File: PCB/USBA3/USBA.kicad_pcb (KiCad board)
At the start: 2 copper layers, 70 x 70 mm, 20 parts, among them J1 USB_A, U1 ESP32-PICO-MINI-02, U2 Barcode, U3 CH340X, U4 QR, U5 MD8942, U6 SHT40

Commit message: Order
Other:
- board text removed: "JLCJLCJLC"

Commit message: Tweak
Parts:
- R10: value 40k2 -> 39k2
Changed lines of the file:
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@@
         (effects (font (size 1 1) (thickness 0.15)))
     )
-    (fp_text value "40k2" (at 0 1.1 90 unlocked) (layer "F.Fab") hide
+    (fp_text value "39k2" (at 0 1.1 90 unlocked) (layer "F.Fab") hide
         (effects (font (size 1 1) (thickness 0.15)))
     )

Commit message: Library update
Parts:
- moved U6 0.36 mm to (94.7, 85.5)
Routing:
- net +3.3V: track 27.5 -> 28.0 mm
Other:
- board text added: "Made in China by JLCPCB"
- board text added: "SDA:20 SCL:7 RGB:22/21/19"
- board text removed: "${TITLE}"
- board text removed: "SDA: 20 SCL: 7 RGB: 22/21/19"
- board text removed: "This is an assembled printed circuit board. This is a component, with no case or leads. Snap off any extra blank panels. Use this part for your own projects as you wish. Made in China for Andrews & Arnold Ltd."
- board text removed: "usba.revk.uk"
- board text removed: "®"

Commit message: Swapped around a bit
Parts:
- moved R11 6.59 mm to (100.3, 82.8), turned to 90 degrees
- moved R9 6.55 mm to (102.8, 81.7), turned to 0 degrees
- moved L2 6.45 mm to (102.8, 88.2), turned to 0 degrees
- moved R10 6.37 mm to (105.3, 82.8), turned to -90 degrees
- moved C6 5.15 mm to (100.3, 84.8), turned to 90 degrees
- moved C7 4.85 mm to (105.3, 84.8)
- moved C4 3.27 mm to (98.2, 83.4), turned to 180 degrees
- moved U5 2.75 mm to (102.8, 83.5), turned to 0 degrees
- moved C8 1.26 mm to (102.8, 85.5), turned to 0 degrees
- moved U3 0.45 mm to (97.8, 87.2)
- moved U6 0.43 mm to (94.8, 85.9)
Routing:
- net DC: track 13.1 -> 16.5 mm
- net GND: track 8.17 -> 5.95 mm, vias 4 -> 6
- net +3.3V: track 28.0 -> 28.8 mm
- net Net-(J1-D-): track 10.7 -> 9.93 mm
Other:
- board text added: "RGB: 22/21/19"
- board text added: "SDA:20 SCL:7"
- board text removed: "SDA:20 SCL:7 RGB:22/21/19"

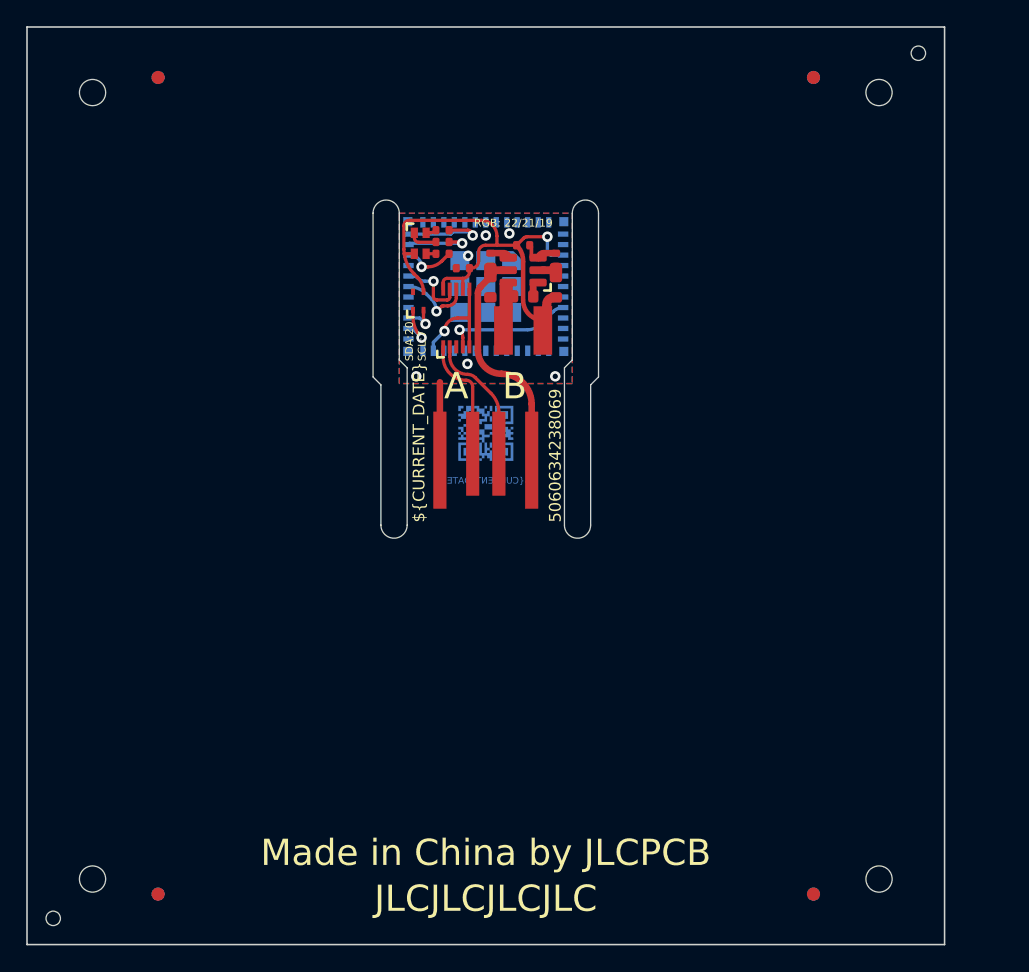
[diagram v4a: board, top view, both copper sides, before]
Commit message: Started rework for single sided
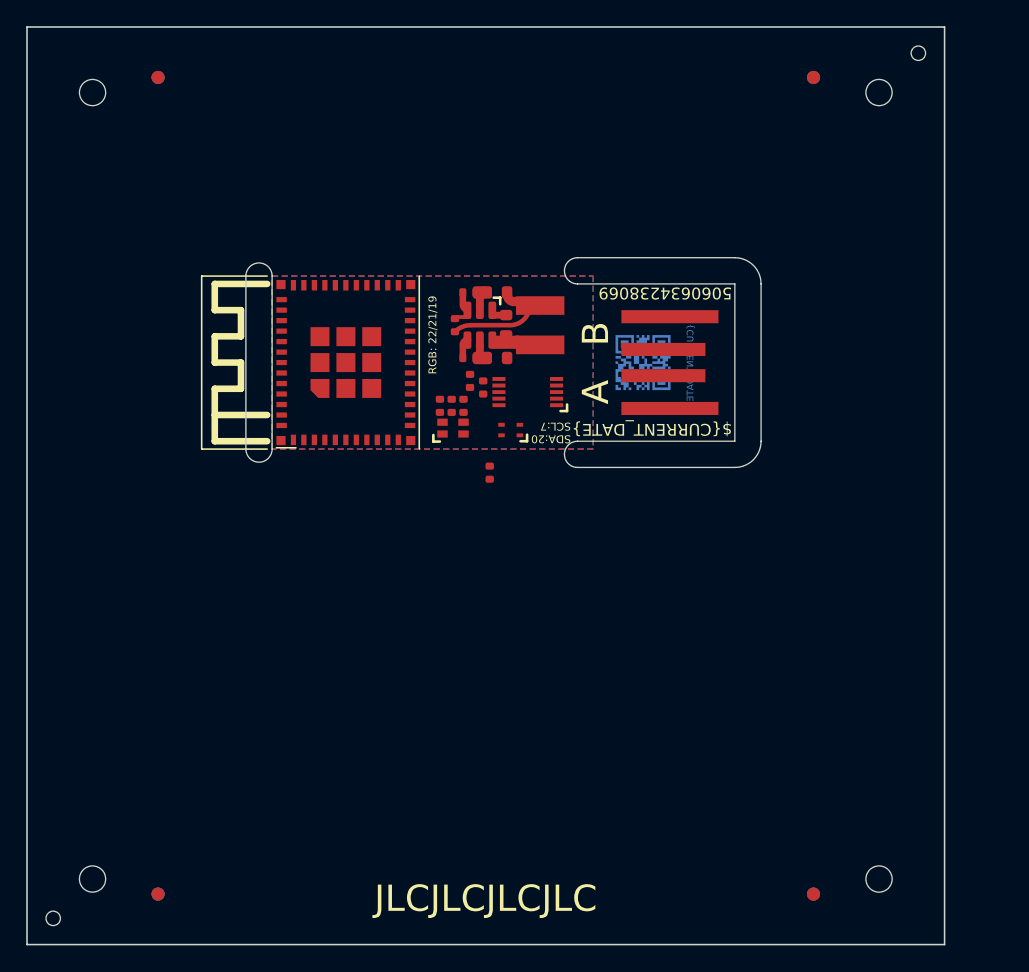
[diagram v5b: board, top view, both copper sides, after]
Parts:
- added C2: 10nF, RevK:C_0402, F.Cu at (100.3, 99.0)
- added C3: 100nF, RevK:C_0402, F.Cu at (99.8, 92.5)
- added V1: 70, RevK:VCUT70, F.Cu at (100.0, 84.0)
- added V2: 70, RevK:VCUT70, F.Cu at (100.0, 97.2)
- U1: moved to F.Cu
- moved J1 22.7 mm to (119.0, 90.6), turned to 90 degrees
- moved D2 14.3 mm to (97.5, 95.6), turned to 0 degrees
- moved R5 13.4 mm to (96.5, 93.9), turned to 90 degrees
- moved U4 13.2 mm to (112.0, 90.6), turned to -90 degrees
- moved R4 12.5 mm to (97.4, 93.9), turned to 90 degrees
- moved U1 12.1 mm to (89.3, 90.6), turned to 90 degrees
- moved U6 12.1 mm to (101.9, 95.8), turned to 180 degrees
- moved R7 11.7 mm to (98.3, 93.9), turned to 90 degrees
- moved C4 8.62 mm to (98.8, 92.0), turned to -90 degrees
- moved R9 8.02 mm to (97.7, 87.8), turned to 90 degrees
- moved U3 7.85 mm to (103.2, 92.8), turned to 180 degrees
- moved R11 7.67 mm to (98.8, 90.2), turned to 180 degrees
- moved R10 7.06 mm to (98.8, 85.2), turned to 0 degrees
- moved C6 5.42 mm to (100.8, 90.2), turned to 180 degrees
- moved U5 5.34 mm to (99.5, 87.8), turned to 90 degrees
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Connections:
- J1 pad 1: DC -> VBUS
- U3 pad 10: +3.3V -> Net-(U3-V3)
- U3 pad 7: +3.3V -> VBUS
- U5 pad 5: DC -> VBUS
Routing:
- net +3.3V: track 28.8 -> 0.00 mm, vias 1 -> 0
- net DC: track 16.5 -> 0.00 mm
- net Net-(J1-D-): track 9.93 -> 0.00 mm
- net EN: track 9.40 -> 0.00 mm, vias 1 -> 0
- net Net-(J1-D+): track 9.34 -> 0.00 mm
- net GPIO0: track 8.68 -> 0.00 mm, vias 1 -> 0
- net G: track 7.16 -> 0.00 mm, vias 1 -> 0
- net GND: track 5.95 -> 0.00 mm, vias 6 -> 0
- net I: track 5.73 -> 0.00 mm, vias 1 -> 0
- net O: track 5.30 -> 0.00 mm, vias 1 -> 0
- net R: track 5.21 -> 0.00 mm, vias 1 -> 0
- net B: track 3.82 -> 0.00 mm, vias 1 -> 0
- net SDA: track 3.55 -> 0.00 mm, vias 1 -> 0
- net SCL: track 2.60 -> 0.00 mm, vias 1 -> 0
- net Net-(D2-RK): track 2.19 -> 0.00 mm
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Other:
- board text removed: "Made in China by JLCPCB"

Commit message: New layout
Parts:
- added C1: 22uF, RevK:C_0402, F.Cu at (99.1, 91.3)
- V1, V2: moved to B.Cu
- moved C4 8.46 mm to (103.2, 84.8), turned to 0 degrees
- moved C2 4.55 mm to (99.6, 94.5)
- moved C3 0.73 mm to (99.1, 92.3), turned to 0 degrees
- turned V1 to 180 degrees
- turned V2 to 0 degrees
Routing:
- net SCL: track 0.00 -> 34.4 mm, vias 0 -> 2
- net +3.3V: track 0.00 -> 29.0 mm, vias 0 -> 2
- net SDA: track 0.00 -> 25.8 mm, vias 0 -> 2
- net G: track 0.00 -> 22.4 mm, vias 0 -> 2
- net O: track 0.00 -> 20.6 mm, vias 0 -> 2
- net GPIO0: track 0.00 -> 20.2 mm, vias 0 -> 2
- net B: track 0.00 -> 18.8 mm, vias 0 -> 2
- net I: track 0.00 -> 18.8 mm, vias 0 -> 2
- net EN: track 0.00 -> 18.3 mm, vias 0 -> 2
- net R: track 0.00 -> 17.9 mm, vias 0 -> 2
- net VBUS: track 0.00 -> 16.6 mm
- net Net-(J1-D+): track 0.00 -> 9.08 mm
- net GND: track 0.00 -> 8.01 mm, vias 0 -> 7
- net Net-(J1-D-): track 0.00 -> 7.35 mm
- net Net-(D2-RK): track 0.00 -> 2.31 mm
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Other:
- board text added: "Made in China for Andrews&Arnold Ltd"
- board text added: "usba.revk.uk"
